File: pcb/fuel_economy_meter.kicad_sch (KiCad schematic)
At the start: 14 parts, among them J1 Conn_01x02_Female, J2 Conn_01x02_Female, U1 MAX9924UAUB+T, U2 ESP32-DEVKIT-V1

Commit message: Remove VR sensor circuit
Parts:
- removed C1: 1nF, Capacitor_SMD:C_1206_3216Metric_Pad1.33x1.80mm_HandSolder, symbol Device:C
- removed R1, R2, R3: 10K, Resistor_SMD:R_1206_3216Metric_Pad1.30x1.75mm_HandSolder, symbol Device:R
- removed U1: MAX9924UAUB+T, Package_SO_Custom:SOP50P490X110-10N, symbol MAX9924:MAX9924UAUB+T
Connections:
- net GND: now also J2.2 (Pin_2)
- net INJ_SIG: now reaches D1.1 (K), R4.1, U2.5 (D4)
- net VSS_OUT: no longer names the net of U2.9 (D18)
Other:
- moved on the sheet: C2, D2, R5, R6

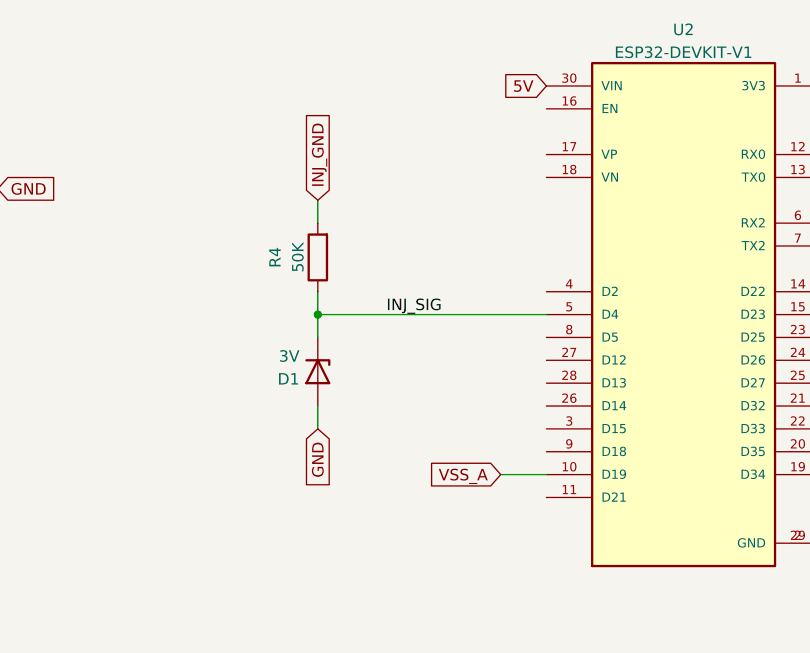
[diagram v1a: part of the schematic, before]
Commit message: Don't use strapping pin for injector signal
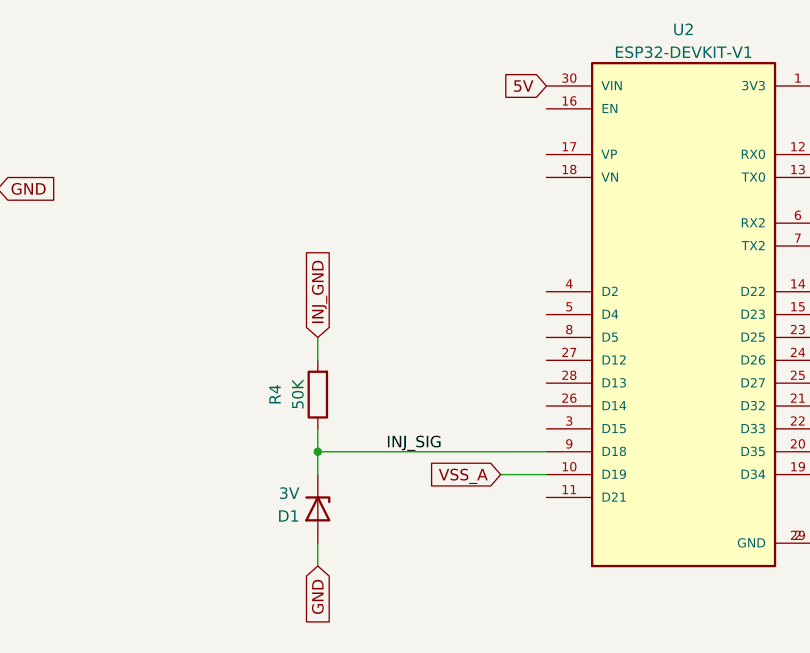
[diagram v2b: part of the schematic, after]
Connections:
- net INJ_SIG: now also U2.9 (D18); no longer U2.5 (D4)
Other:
- moved on the sheet: D1, R4
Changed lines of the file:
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@@
   (junction (at 104.14 31.75) (diameter 0) (color 0 0 0 0)
   )
+  (junction (at 142.24 66.04) (diameter 0) (color 0 0 0 0)
+  )
   (junction (at 83.82 33.02) (diameter 0) (color 0 0 0 0)
   )
-  (junction (at 142.24 50.8) (diameter 0) (color 0 0 0 0)
-  )
   (wire (pts (xy 104.14 36.83) (xy 106.68 36.83))
     (stroke (width 0) (type default) (color 0 0 0 0))
@@
     (stroke (width 0) (type default) (color 0 0 0 0))
   )
-  (wire (pts (xy 142.24 50.8) (xy 142.24 53.34))
-    (stroke (width 0) (type default) (color 0 0 0 0))
-  )
   (wire (pts (xy 93.98 36.83) (xy 93.98 39.37))
     (stroke (width 0) (type default) (color 0 0 0 0))
   )
-  (wire (pts (xy 142.24 60.96) (xy 142.24 63.5))
+  (wire (pts (xy 142.24 76.2) (xy 142.24 78.74))
     (stroke (width 0) (type default) (color 0 0 0 0))
   )
@@
     (stroke (width 0) (type default) (color 0 0 0 0))
   )
+  (wire (pts (xy 142.24 66.04) (xy 142.24 68.58))
+    (stroke (width 0) (type default) (color 0 0 0 0))
+  )
   (wire (pts (xy 80.01 33.02) (xy 83.82 33.02))
     (stroke (width 0) (type default) (color 0 0 0 0))
@@
     (stroke (width 0) (type default) (color 0 0 0 0))
   )
-  (wire (pts (xy 142.24 38.1) (xy 142.24 40.64))
-    (stroke (width 0) (type default) (color 0 0 0 0))
-  )
-  (wire (pts (xy 142.24 50.8) (xy 167.64 50.8))
-    (stroke (width 0) (type default) (color 0 0 0 0))
-  )
-  (wire (pts (xy 142.24 48.26) (xy 142.24 50.8))
+  (wire (pts (xy 142.24 53.34) (xy 142.24 55.88))
+    (stroke (width 0) (type default) (color 0 0 0 0))
+  )
+  (wire (pts (xy 142.24 66.04) (xy 167.64 66.04))
+    (stroke (width 0) (type default) (color 0 0 0 0))
+  )
+  (wire (pts (xy 142.24 63.5) (xy 142.24 66.04))
     (stroke (width 0) (type default) (color 0 0 0 0))
   )
@@
     (stroke (width 0) (type default) (color 0 0 0 0))
   )
-  (label "INJ_SIG" (at 149.86 50.8 0)
+  (label "INJ_SIG" (at 149.86 66.04 0)
     (effects (font (size 1.27 1.27)) (justify left bottom))
   )
@@
     )
   )
-  (global_label "INJ_GND" (shape input) (at 142.24 38.1 90) (fields_autoplaced)
-    (effects (font (size 1.27 1.27)) (justify left))
-    (property "Intersheet References" "${INTERSHEET_REFS}" (id 0) (at 142.1606 28.0348 90)
+  (global_label "INJ_GND" (shape input) (at 142.24 53.34 90) (fields_autoplaced)
+    (effects (font (size 1.27 1.27)) (justify left))
+    (property "Intersheet References" "${INTERSHEET_REFS}" (id 0) (at 142.1606 43.2748 90)
       (effects (font (size 1.27 1.27)) (justify left) hide)
     )
@@
     )
   )
-  (global_label "GND" (shape input) (at 142.24 63.5 270) (fields_autoplaced)
-    (effects (font (size 1.27 1.27)) (justify right))
-    (property "Intersheet References" "${INTERSHEET_REFS}" (id 0) (at 218.44 -102.87 0)
+  (global_label "GND" (shape input) (at 142.24 78.74 270) (fields_autoplaced)
+    (effects (font (size 1.27 1.27)) (justify right))
+    (property "Intersheet References" "${INTERSHEET_REFS}" (id 0) (at 218.44 -87.63 0)
       (effects (font (size 1.27 1.27)) hide)
     )
@@
     (pin "2")
   )
-  (symbol (lib_id "Device:D_Zener") (at 142.24 57.15 270) (unit 1)
-    (in_bom yes) (on_board yes) (fields_autoplaced)
-    (property "Reference" "D1" (id 0) (at 140.208 57.9847 90)
-      (effects (font (size 1.27 1.27)) (justify right))
-    )
-    (property "Value" "3V" (id 1) (at 140.208 55.4478 90)
-      (effects (font (size 1.27 1.27)) (justify right))
-    )
-    (property "Footprint" "Diode_SMD:D_SOD-123" (id 2) (at 142.24 57.15 0)
-      (effects (font (size 1.27 1.27)) hide)
-    )
-    (property "Datasheet" "~" (id 3) (at 142.24 57.15 0)
+  (symbol (lib_id "Device:D_Zener") (at 142.24 72.39 270) (unit 1)
+    (in_bom yes) (on_board yes) (fields_autoplaced)
+    (property "Reference" "D1" (id 0) (at 140.208 73.2247 90)
+      (effects (font (size 1.27 1.27)) (justify right))
+    )
+    (property "Value" "3V" (id 1) (at 140.208 70.6878 90)
+      (effects (font (size 1.27 1.27)) (justify right))
+    )
+    (property "Footprint" "Diode_SMD:D_SOD-123" (id 2) (at 142.24 72.39 0)
+      (effects (font (size 1.27 1.27)) hide)
+    )
+    (property "Datasheet" "~" (id 3) (at 142.24 72.39 0)
       (effects (font (size 1.27 1.27)) hide)
     )
@@
     (pin "2")
   )
-  (symbol (lib_id "Device:R") (at 142.24 44.45 180) (unit 1)
-    (in_bom yes) (on_board yes) (fields_autoplaced)
-    (property "Reference" "R4" (id 0) (at 137.5242 44.45 90))
-    (property "Value" "50K" (id 1) (at 140.0611 44.45 90))
-    (property "Footprint" "Resistor_SMD:R_1206_3216Metric_Pad1.30x1.75mm_HandSolder" (id 2) (at 144.018 44.45 90)
-      (effects (font (size 1.27 1.27)) hide)
-    )
-    (property "Datasheet" "~" (id 3) (at 142.24 44.45 0)
-      (effects (font (size 1.27 1.27)) hide)
-    )
+  (symbol (lib_id "Device:R") (at 142.24 59.69 180) (unit 1)
+    (in_bom yes) (on_board yes) (fields_autoplaced)
+    (property "Reference" "R4" (id 0) (at 137.5242 59.69 90))
+    (property "Value" "50K" (id 1) (at 140.0611 59.69 90))
+    (property "Footprint" "Resistor_SMD:R_1206_3216Metric_Pad1.30x1.75mm_HandSolder" (id 2) (at 144.018 59.69 90)
+      (effects (font (size 1.27 1.27)) hide)
+    )
+    (property "Datasheet" "~" (id 3) (at 142.24 59.69 0)
+      (effects (font (size 1.27 1.27)) hide)
+    )

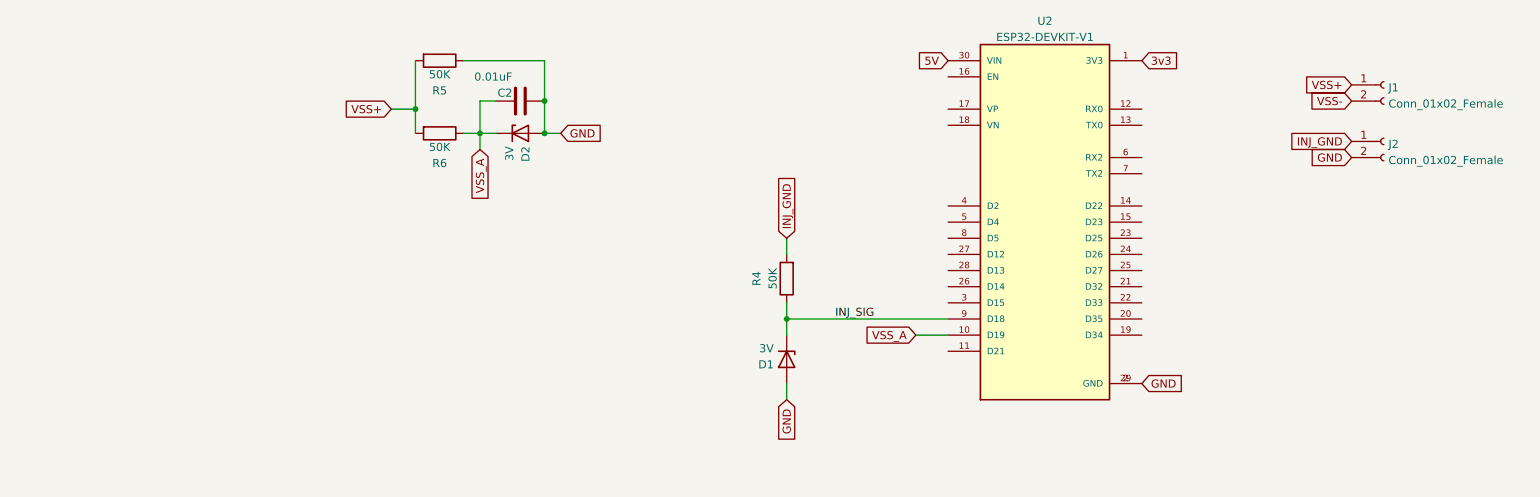
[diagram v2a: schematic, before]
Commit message: Consolidate component designators
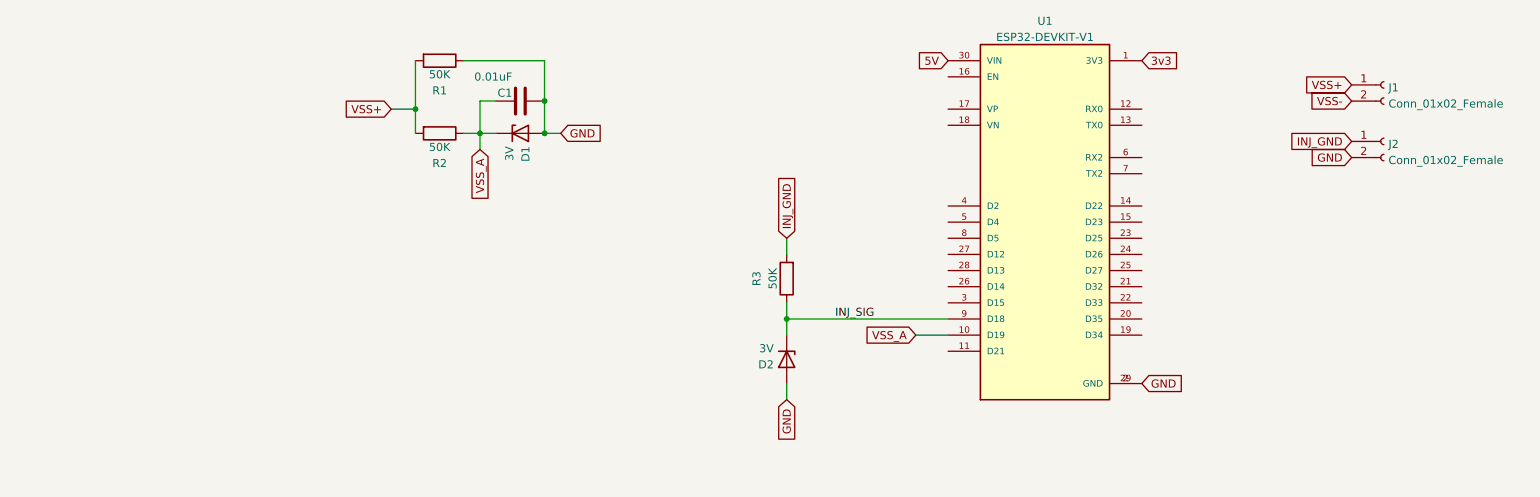
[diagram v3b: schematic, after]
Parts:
- renumbered C2 to C1, D2 to D1, D1 to D2, R5 to R1, R6 to R2, R4 to R3, U2 to U1
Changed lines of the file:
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@@
   (symbol (lib_id "Device:C") (at 100.33 31.75 90) (unit 1)
     (in_bom yes) (on_board yes)
-    (property "Reference" "C2" (id 0) (at 99.06 30.4769 90)
+    (property "Reference" "C1" (id 0) (at 99.06 30.4769 90)
       (effects (font (size 1.27 1.27)) (justify left))
     )
@@
   (symbol (lib_id "Device:D_Zener") (at 142.24 72.39 270) (unit 1)
     (in_bom yes) (on_board yes) (fields_autoplaced)
-    (property "Reference" "D1" (id 0) (at 140.208 73.2247 90)
+    (property "Reference" "D2" (id 0) (at 140.208 73.2247 90)
       (effects (font (size 1.27 1.27)) (justify right))
     )
@@
   (symbol (lib_id "Device:R") (at 87.63 36.83 270) (unit 1)
     (in_bom yes) (on_board yes) (fields_autoplaced)
-    (property "Reference" "R6" (id 0) (at 87.63 41.5458 90))
+    (property "Reference" "R2" (id 0) (at 87.63 41.5458 90))
     (property "Value" "50K" (id 1) (at 87.63 39.0089 90))
     (property "Footprint" "Resistor_SMD:R_1206_3216Metric_Pad1.30x1.75mm_HandSolder" (id 2) (at 87.63 35.052 90)
@@
   (symbol (lib_id "Device:D_Zener") (at 100.33 36.83 0) (unit 1)
     (in_bom yes) (on_board yes) (fields_autoplaced)
-    (property "Reference" "D2" (id 0) (at 101.1647 38.862 90)
+    (property "Reference" "D1" (id 0) (at 101.1647 38.862 90)
       (effects (font (size 1.27 1.27)) (justify right))
     )
@@
   (symbol (lib_id "Device:R") (at 142.24 59.69 180) (unit 1)
     (in_bom yes) (on_board yes) (fields_autoplaced)
-    (property "Reference" "R4" (id 0) (at 137.5242 59.69 90))
+    (property "Reference" "R3" (id 0) (at 137.5242 59.69 90))
     (property "Value" "50K" (id 1) (at 140.0611 59.69 90))
     (property "Footprint" "Resistor_SMD:R_1206_3216Metric_Pad1.30x1.75mm_HandSolder" (id 2) (at 144.018 59.69 90)
@@
   (symbol (lib_id "Device:R") (at 87.63 25.4 270) (unit 1)
     (in_bom yes) (on_board yes) (fields_autoplaced)
-    (property "Reference" "R5" (id 0) (at 87.63 30.1158 90))
+    (property "Reference" "R1" (id 0) (at 87.63 30.1158 90))
     (property "Value" "50K" (id 1) (at 87.63 27.5789 90))
     (property "Footprint" "Resistor_SMD:R_1206_3216Metric_Pad1.30x1.75mm_HandSolder" (id 2) (at 87.63 23.622 90)
@@
   (symbol (lib_id "ESP32_Devkit:ESP32-DEVKIT-V1") (at 182.88 50.8 0) (unit 1)
     (in_bom yes) (on_board yes) (fields_autoplaced)
-    (property "Reference" "U2" (id 0) (at 182.88 19.1602 0))
+    (property "Reference" "U1" (id 0) (at 182.88 19.1602 0))
     (property "Value" "ESP32-DEVKIT-V1" (id 1) (at 182.88 21.6971 0))
     (property "Footprint" "ESP32_Devkit:MODULE_ESP32_DEVKIT_V1" (id 2) (at 182.88 50.8 0)
@@
   (symbol_instances
     (path "/584f502d-9d89-4574-81cb-04c8a3a6d3de"
-      (reference "C2") (unit 1) (value "0.01uF") (footprint "Capacitor_SMD:C_1206_3216Metric_Pad1.33x1.80mm_HandSolder")
+      (reference "C1") (unit 1) (value "0.01uF") (footprint "Capacitor_SMD:C_1206_3216Metric_Pad1.33x1.80mm_HandSolder")
+    )
+    (path "/dcd1ae19-5b31-4307-be70-5d1edee18fb2"
+      (reference "D1") (unit 1) (value "3V") (footprint "Diode_SMD:D_SOD-123")
     )
     (path "/62ec3c16-b777-42de-8733-6fc54a481a12"
-      (reference "D1") (unit 1) (value "3V") (footprint "Diode_SMD:D_SOD-123")
-    )
-    (path "/dcd1ae19-5b31-4307-be70-5d1edee18fb2"
       (reference "D2") (unit 1) (value "3V") (footprint "Diode_SMD:D_SOD-123")
     )
@@
       (reference "J2") (unit 1) (value "Conn_01x02_Female") (footprint "Connector_JST:JST_XH_B2B-XH-A_1x02_P2.50mm_Vertical")
     )
+    (path "/f29a79cd-94fc-4fdd-91fe-0945a7276a6b"
+      (reference "R1") (unit 1) (value "50K") (footprint "Resistor_SMD:R_1206_3216Metric_Pad1.30x1.75mm_HandSolder")
+    )
+    (path "/76b7f11b-38aa-483a-8520-a14eca6a2c2a"
+      (reference "R2") (unit 1) (value "50K") (footprint "Resistor_SMD:R_1206_3216Metric_Pad1.30x1.75mm_HandSolder")
+    )
     (path "/dd91dc67-4903-4b53-ab60-5b602c406e3d"
-      (reference "R4") (unit 1) (value "50K") (footprint "Resistor_SMD:R_1206_3216Metric_Pad1.30x1.75mm_HandSolder")
-    )
-    (path "/f29a79cd-94fc-4fdd-91fe-0945a7276a6b"
-      (reference "R5") (unit 1) (value "50K") (footprint "Resistor_SMD:R_1206_3216Metric_Pad1.30x1.75mm_HandSolder")
-    )
-    (path "/76b7f11b-38aa-483a-8520-a14eca6a2c2a"
-      (reference "R6") (unit 1) (value "50K") (footprint "Resistor_SMD:R_1206_3216Metric_Pad1.30x1.75mm_HandSolder")
+      (reference "R3") (unit 1) (value "50K") (footprint "Resistor_SMD:R_1206_3216Metric_Pad1.30x1.75mm_HandSolder")
     )
     (path "/f621143c-13d3-4a78-902b-8ef71313a59a"
-      (reference "U2") (unit 1) (value "ESP32-DEVKIT-V1") (footprint "ESP32_Devkit:MODULE_ESP32_DEVKIT_V1")
-    )
-  )
+      (reference "U1") (unit 1) (value "ESP32-DEVKIT-V1") (footprint "ESP32_Devkit:MODULE_ESP32_DEVKIT_V1")
+    )
+  )
